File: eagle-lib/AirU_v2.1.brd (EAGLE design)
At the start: 71.1 x 79.4 mm, 86 parts, among them Q1 BSS138W-7-F, Q2 MMBT3904LT1G, Q3 MMBT3904LT1G, Q5 NCE3407A, U1 HDC1080DMBT, U2 CH340T-SSOP20, U3 CJT1117-3.3-SOT223, U4 MAX2659-DFN6, U5 L70-M39, U6 MOLEX-53261-0871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

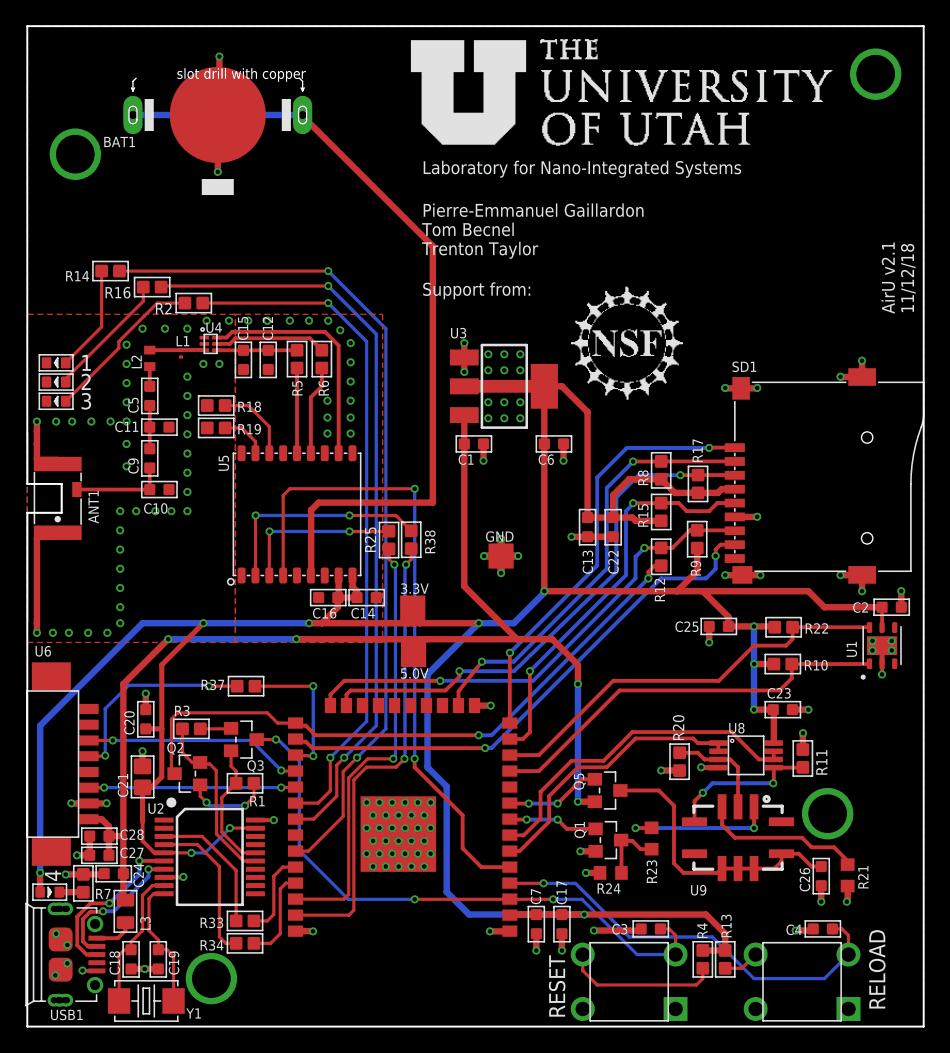
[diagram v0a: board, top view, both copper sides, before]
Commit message: updated board
changed PM_RESET to an RTC GPIO (previously unpopulated), and changed the logo/revision info
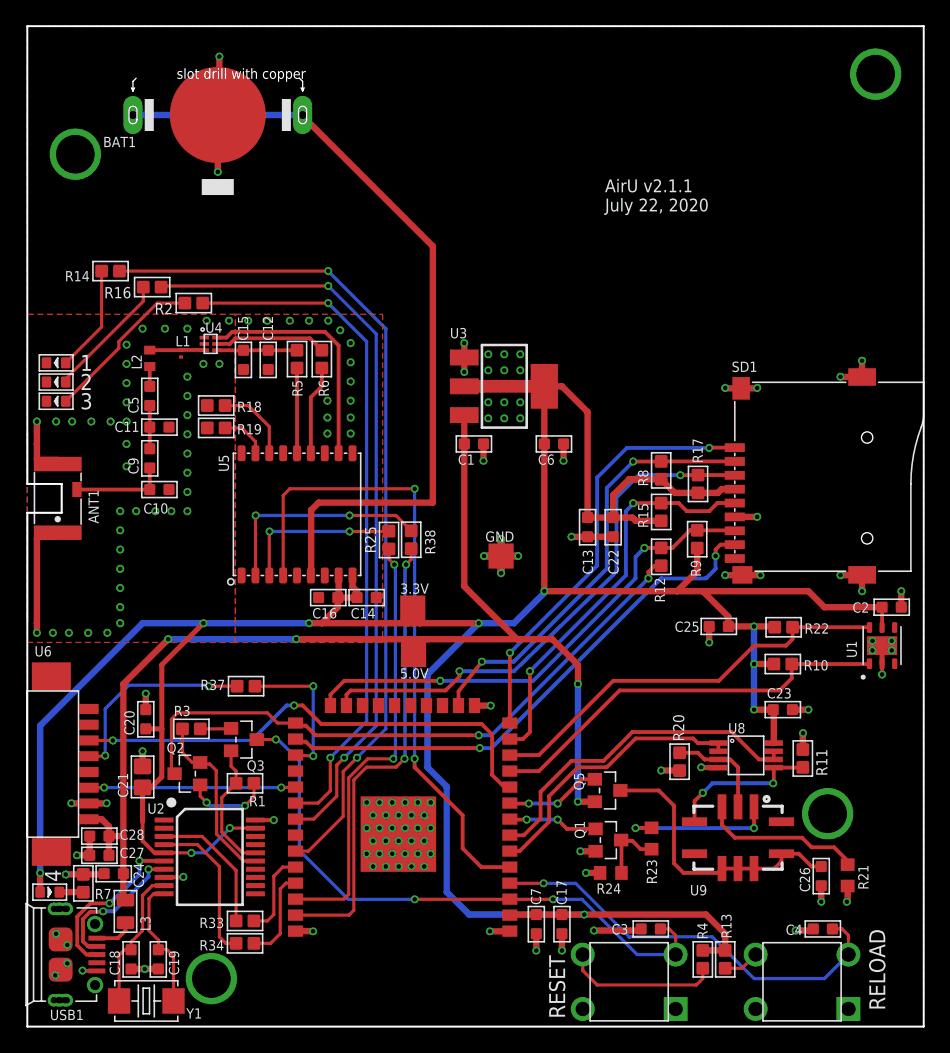
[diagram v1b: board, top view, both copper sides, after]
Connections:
- net PM_RESET: now also U7.10; no longer U7.28
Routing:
- net PM_RESET: track 17.4 -> 39.1 mm
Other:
- board text added: "AirU v2.1.1 July 22, 2020"
- board text removed: "AirU v2.1 11/12/18"
- board text removed: "Laboratory for Nano-Integrated Systems"
- board text removed: "Pierre-Emmanuel Gaillardon Tom Becnel Trenton Taylor"
- board text removed: "Support from:"
